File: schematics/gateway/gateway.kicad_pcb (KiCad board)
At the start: 2 copper layers, 120 x 80 mm, 12 parts, among them J1 Power, J2 PN532_Port, J4 Button_Port

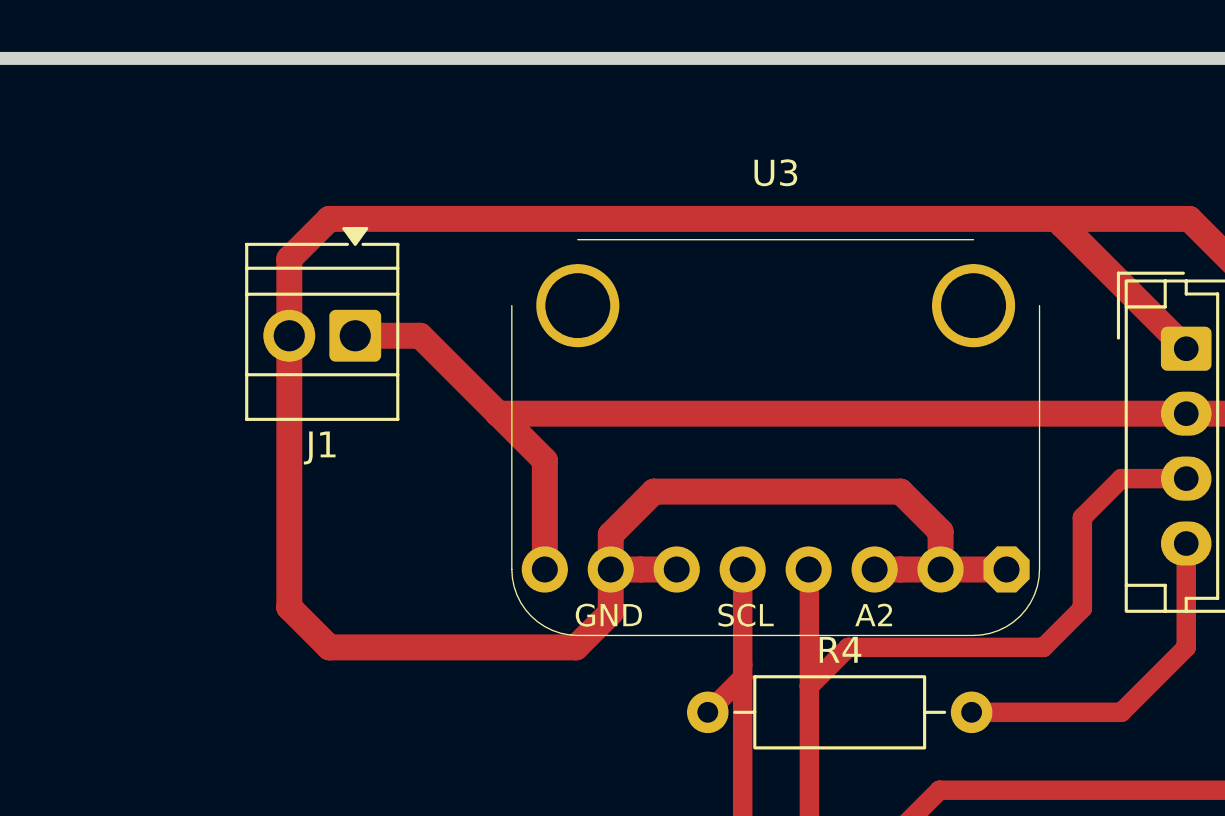
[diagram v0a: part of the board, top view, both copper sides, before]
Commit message: adjust pad sizes for easier drilling and soldering
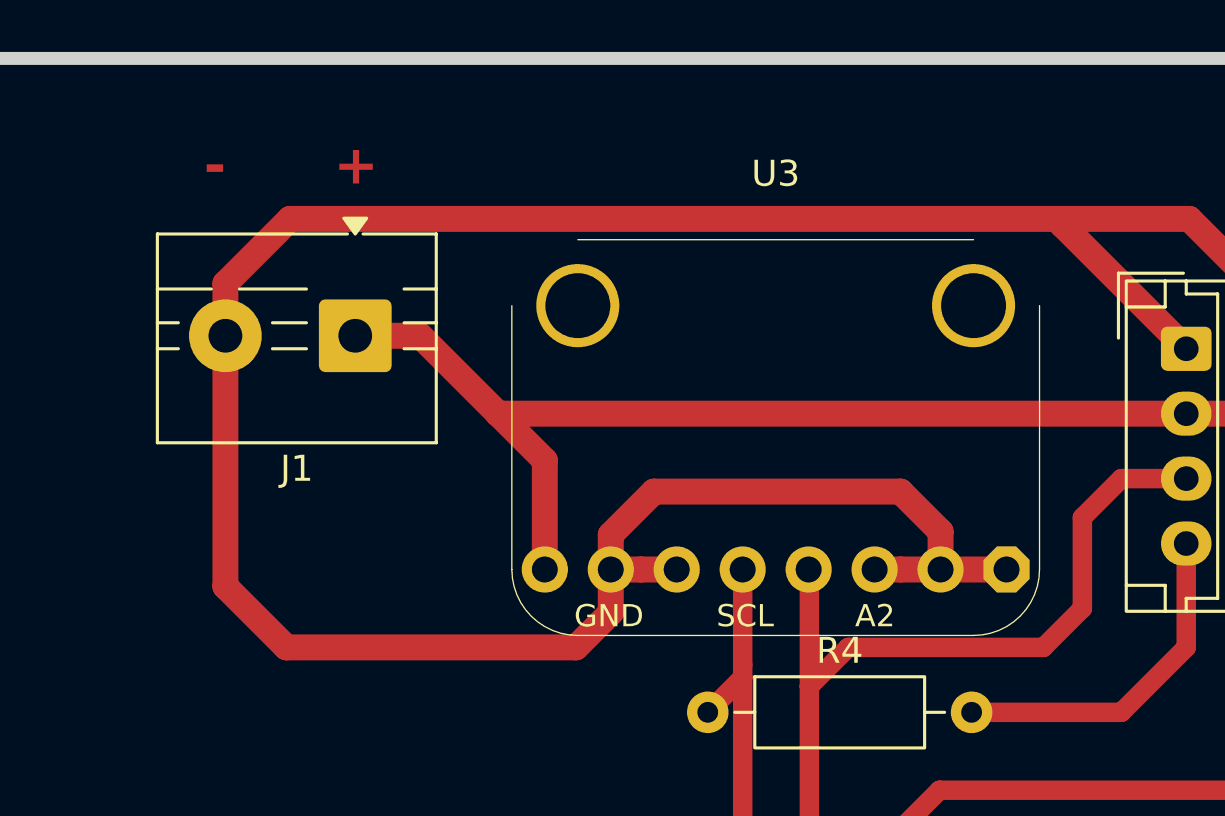
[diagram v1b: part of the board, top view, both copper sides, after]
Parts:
- J1: footprint TerminalBlock:TerminalBlock_Xinya_XY308-2.54-2P_1x02_P2.54mm_Horizontal -> TerminalBlock:TerminalBlock_MaiXu_MX126-5.0-02P_1x02_P5.00mm
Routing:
- net GND: track 117.2 -> 121.1 mm
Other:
- board text added: "+"
- board text added: "-"
